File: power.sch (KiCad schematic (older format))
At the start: 25 parts, among them Q1 DMP3099L-7, U3 TPS565201DDC, U5 MCP73223-C2S

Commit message: readability
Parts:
- added J?: Conn_01x02_Male, Connector_JST:JST_SH_BM02B-SRSS-TB_1x02-1MP_P1.00mm_Vertical, symbol Connector:Conn_01x02_Male
- added J?: Conn_01x02_Male, Connector_JST:JST_SH_SM02B-SRSS-TB_1x02-1MP_P1.00mm_Horizontal, symbol Connector:Conn_01x02_Male
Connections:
- net GND: now also J?.2 (Pin_2), J?.2 (Pin_2)
- net VBAT: now also J?.1 (Pin_1), J?.1 (Pin_1)
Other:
- note added: "2 redundant battery connectors.\nconnect only one!"
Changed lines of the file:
@@
 $Descr A4 11693 8268
 encoding utf-8
-Sheet 2 2
+Sheet 2 5
 Title ""
 Date ""
@@
 Wire Wire Line
 	6450 4700 6700 4700
+$Comp
+L Connector:Conn_01x02_Male J?
+U 1 1 606051B8
+P 9800 3600
+F 0 "J?" H 9908 3781 50  0000 C CNN
+F 1 "Conn_01x02_Male" H 9908 3690 50  0000 C CNN
+F 2 "Connector_JST:JST_SH_BM02B-SRSS-TB_1x02-1MP_P1.00mm_Vertical" H 9800 3600 50  0001 C CNN
+F 3 "~" H 9800 3600 50  0001 C CNN
+	1    9800 3600
+	1    0    0    -1
+$EndComp
+Wire Wire Line
+	10000 2800 10000 3600
+Text GLabel 10000 2800 1    118  Input ~ 0
+VBAT
+Wire Wire Line
+	10000 3700 10000 4400
+$Comp
+L power:GND #PWR?
+U 1 1 606051C1
+P 10000 4400
+F 0 "#PWR?" H 10000 4150 50  0001 C CNN
+F 1 "GND" H 10005 4227 50  0000 C CNN
+F 2 "" H 10000 4400 50  0001 C CNN
+F 3 "" H 10000 4400 50  0001 C CNN
+	1    10000 4400
+	1    0    0    -1
+$EndComp
+$Comp
+L Connector:Conn_01x02_Male J?
+U 1 1 606051C7
+P 10600 3600
+F 0 "J?" H 10708 3781 50  0000 C CNN
+F 1 "Conn_01x02_Male" H 10708 3690 50  0000 C CNN
+F 2 "Connector_JST:JST_SH_SM02B-SRSS-TB_1x02-1MP_P1.00mm_Horizontal" H 10600 3600 50  0001 C CNN
+F 3 "~" H 10600 3600 50  0001 C CNN
+	1    10600 3600
+	1    0    0    -1
+$EndComp
+Wire Wire Line
+	10800 2800 10800 3600
+Text GLabel 10800 2800 1    118  Input ~ 0
+VBAT
+Wire Wire Line
+	10800 3700 10800 4400
+$Comp
+L power:GND #PWR?
+U 1 1 606051D0
+P 10800 4400
+F 0 "#PWR?" H 10800 4150 50  0001 C CNN
+F 1 "GND" H 10805 4227 50  0000 C CNN
+F 2 "" H 10800 4400 50  0001 C CNN
+F 3 "" H 10800 4400 50  0001 C CNN
+	1    10800 4400
+	1    0    0    -1
+$EndComp
+Text Notes 9950 2000 0    50   ~ 0
+2 redundant battery connectors.\nconnect only one!
 $EndSCHEMATC

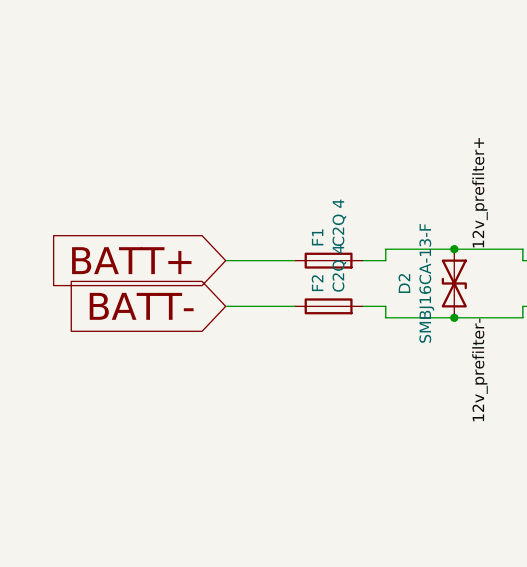
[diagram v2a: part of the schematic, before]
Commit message: Esp32 & Canbus Sch. edited.
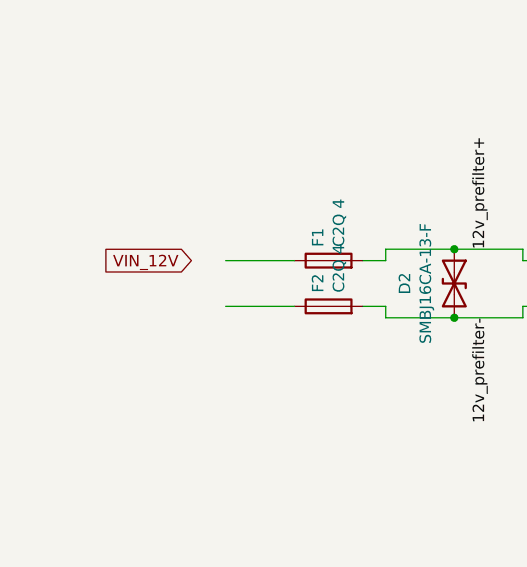
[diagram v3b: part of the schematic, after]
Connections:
- net labels added: VIN_12V
- net labels removed: BATT+, BATT-
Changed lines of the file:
@@
 Wire Wire Line
 	1700 2300 1400 2300
-Text GLabel 1400 2300 0    118  Input ~ 0
-BATT-
-Text GLabel 1400 2100 0    118  Input ~ 0
-BATT+
 Wire Wire Line
 	6900 5000 6900 5150
@@
 Text Notes 9950 2000 0    50   ~ 0
 2 redundant battery connectors.\nconnect only one!
+Text GLabel 1250 2100 0    50   Input ~ 0
+VIN_12V
 $EndSCHEMATC

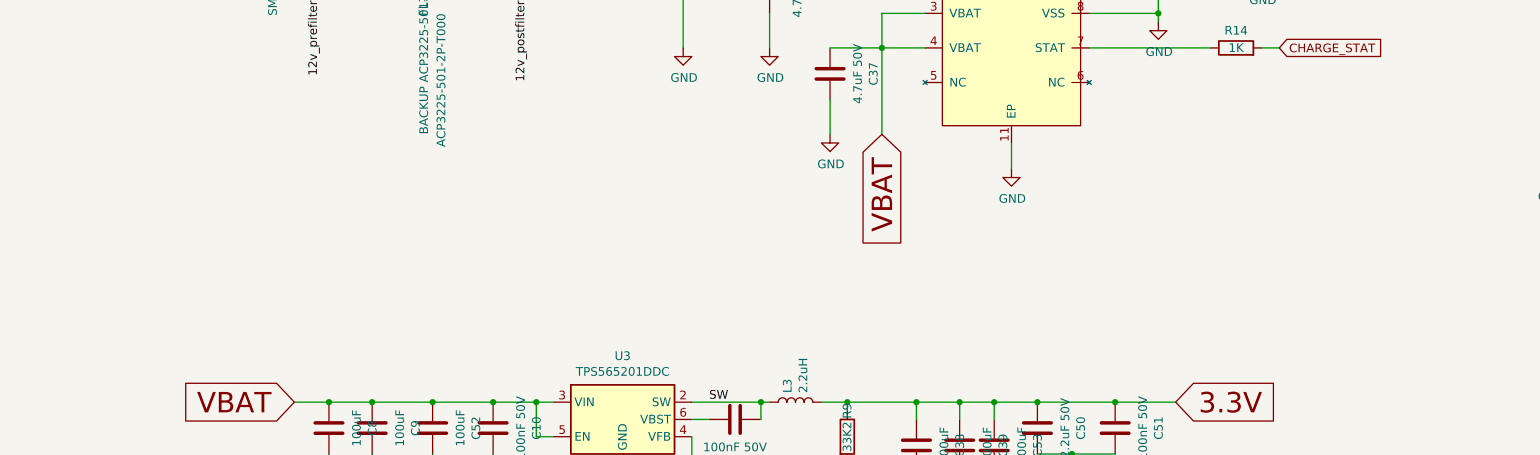
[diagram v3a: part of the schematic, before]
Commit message: Modem schematic updated.
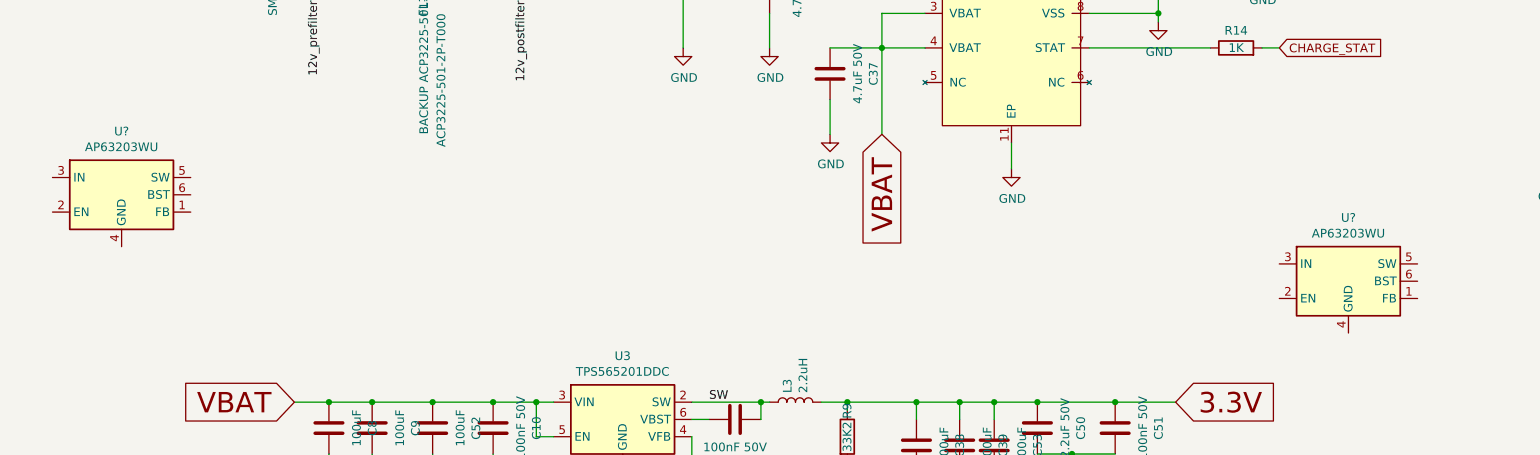
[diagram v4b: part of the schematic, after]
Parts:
- added U? (x2): AP63203WU, Package_TO_SOT_SMD:TSOT-23-6, symbol Regulator_Switching:AP63203WU
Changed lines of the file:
@@
 Text GLabel 1250 2100 0    50   Input ~ 0
 VIN_12V
+$Comp
+L Regulator_Switching:AP63203WU U?
+U 1 1 604E2EDE
+P 1400 3500
+F 0 "U?" H 1400 3867 50  0000 C CNN
+F 1 "AP63203WU" H 1400 3776 50  0000 C CNN
+F 2 "Package_TO_SOT_SMD:TSOT-23-6" H 1400 2600 50  0001 C CNN
+F 3 "https://www.diodes.com/assets/Datasheets/AP63200-AP63201-AP63203-AP63205.pdf" H 1400 3500 50  0001 C CNN
+	1    1400 3500
+	1    0    0    -1
+$EndComp
+$Comp
+L Regulator_Switching:AP63203WU U?
+U 1 1 6069DD08
+P 8500 4000
+F 0 "U?" H 8500 4367 50  0000 C CNN
+F 1 "AP63203WU" H 8500 4276 50  0000 C CNN
+F 2 "Package_TO_SOT_SMD:TSOT-23-6" H 8500 3100 50  0001 C CNN
+F 3 "https://www.diodes.com/assets/Datasheets/AP63200-AP63201-AP63203-AP63205.pdf" H 8500 4000 50  0001 C CNN
+	1    8500 4000
+	1    0    0    -1
+$EndComp
 $EndSCHEMATC

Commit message: Power Sch. Updated.
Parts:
- removed C36, C37: 4.7uF 50V, Capacitor_SMD:C_0603_1608Metric, symbol Device:C
- removed C39, C52, C53, C8: 100uF, Capacitor_SMD:C_1206_3216Metric, symbol Device:C
- removed C51: 100nF 50V, Capacitor_SMD:C_0603_1608Metric, symbol Device:C
- removed F1, F2: C2Q 4, Fuse:Fuse_0603_1608Metric, symbol Device:Fuse
- removed FL2: BACKUP ACP3225-501-2P-T000, aep:ACP3225, symbol Device:EMI_Filter_LL_1423
- removed J?: Conn_01x02_Male, Connector_JST:JST_SH_BM02B-SRSS-TB_1x02-1MP_P1.00mm_Vertical, symbol Connector:Conn_01x02_Male
- removed J?: Conn_01x02_Male, Connector_JST:JST_SH_SM02B-SRSS-TB_1x02-1MP_P1.00mm_Horizontal, symbol Connector:Conn_01x02_Male
- removed L3: 2.2uH, Inductor_SMD:L_Coilcraft_XxL4020, symbol Device:L
- removed Q1: DMP3099L-7, Package_TO_SOT_SMD:SOT-23, symbol Device:Q_PMOS_GSD
- removed R13, R14: 1K, Resistor_SMD:R_0603_1608Metric, symbol Device:R
- removed U3: TPS565201DDC, Package_TO_SOT_SMD:SOT-23-6, symbol Regulator_Switching:TPS565208
- removed U?: AP63203WU, Package_TO_SOT_SMD:TSOT-23-6, symbol Regulator_Switching:AP63203WU
- added C1, C13, C16, C2: 10uF 50V, Capacitor_SMD:C_0805_2012Metric, symbol Device:C
- added C11, C20, C5, C6: 100nF 50V, Capacitor_SMD:C_0603_1608Metric, symbol Device:C
- added C12, C14, C15, C3, C4: 4.7uF, Capacitor_SMD:C_0603_1608Metric, symbol Device:C
- added C17: 100nF, Capacitor_SMD:C_0603_1608Metric, symbol Device:C
- added C19, C21, C23: 22uF 25V, Capacitor_SMD:C_0805_2012Metric, symbol Device:C
- added C22, C24: 100pF 50V, Capacitor_SMD:C_0603_1608Metric, symbol Device:C
- added D2: RS1GTR, Diode_SMD:D_SMA, symbol Device:D_Schottky
- added F1: 0ZCF0030FF2C, Fuse:Fuse_2920_7451Metric_Castellated, symbol Device:Polyfuse_Small
- added J2: Conn_01x02_Male, Connector_JST:JST_SH_BM02B-SRSS-TB_1x02-1MP_P1.00mm_Vertical, symbol Connector:Conn_01x02_Male
- added J3: Conn_01x02_Male, Connector_JST:JST_SH_SM02B-SRSS-TB_1x02-1MP_P1.00mm_Horizontal, symbol Connector:Conn_01x02_Male
- added L1: 1255AY-3R9N=P3, IND_1255AY-3R9N=P3, symbol 1255AY-3R9N_P3:1255AY-3R9N=P3
- added R1, R11, R2, R4: 10k, Resistors:0603, symbol Device:R
- added R10: 3.9k, Resistors:0603, symbol Device:R
- added R3, R5, R7: R0, Resistors:0603, symbol Device:R
- added R6, R8: R0-DNP, Resistors:0603, symbol Device:R
- added TP1, TP2, TP3, TP4, TP5, TP6, TP7: L0, OLIMEX_TestPoints-FP:TP_SMD, symbol Connector:TestPoint_Alt
- added U1, U2: LM66100, Package_TO_SOT_SMD:SOT-363_SC-70-6, symbol pocasicko-cache:Moje_LM66100
- added U3: TLV76750, Package_SON:WSON-6-1EP_2x2mm_P0.65mm_EP1x1.6mm_ThermalVias, symbol aep:TLV767
- C10, C18: value 100nF 50V -> 100nF
- C7: renamed from C50; value 2.2uF 50V -> 100pF 50V
- C8: renamed from C38; value 100uF -> 10uF 50V; footprint Capacitor_SMD:C_1206_3216Metric -> Capacitor_SMD:C_0805_2012Metric
- C9: value 100uF -> 10uF; footprint Capacitor_SMD:C_1206_3216Metric -> Capacitor_SMD:C_0603_1608Metric
- D1: renamed from D2; value SMBJ16CA-13-F -> SMBJ16CA-Q
- R12: value 10K -> 10k; footprint Resistor_SMD:R_0603_1608Metric -> Resistors:0603
- R9: value 33K2 -> R0-DNP; footprint Resistor_SMD:R_0603_1608Metric -> Resistors:0603
- U5: value MCP73223-C2S -> MCP73123-22S
- gave numbers to parts that had none: 1
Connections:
- net labels added: +12V, +3V3, +5V, +BATT, 12V_FILTER_IN, 3V3_BUCK, CHARGER_EN, VIN_GND
- net labels removed: 12v_postfilter+, 12v_postfilter-, 12v_prefilter+, 12v_prefilter-, 3.3V, SW, V12_safe, VBAT
- wire segments 103 -> 138
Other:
- note added: "Batt. Charger 5V Supply"
- note added: "Feedback resistors for \nAP63200 ADJ. Version"
- note added: "LiFePo4 Charger"
- note added: "Main 3V3 Buck Conv."
- note added: "Main Input Filter & Protection"
- note added: "Power Supply Switchover"
- note removed: "TVS clamp to 26V\n"
- moved on the sheet: C7, C8, D1, FL1, U4

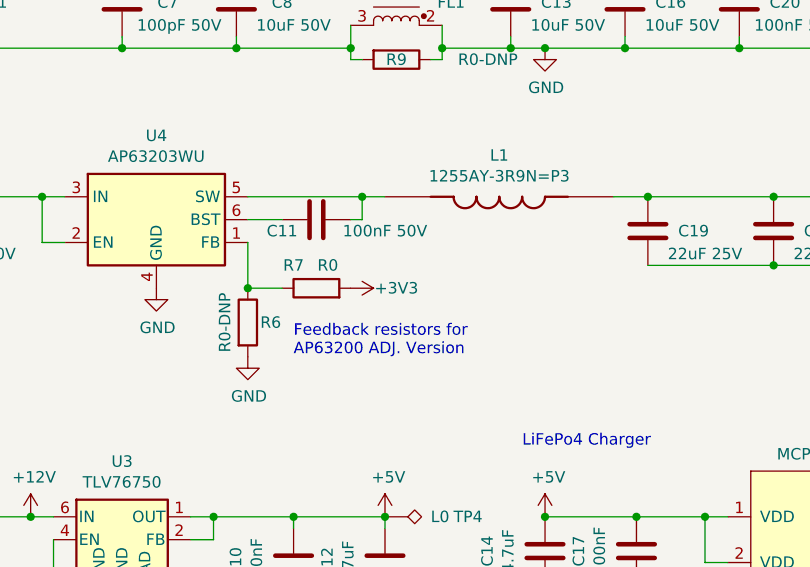
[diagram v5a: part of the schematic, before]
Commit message: Fixed Buck feedback reference.
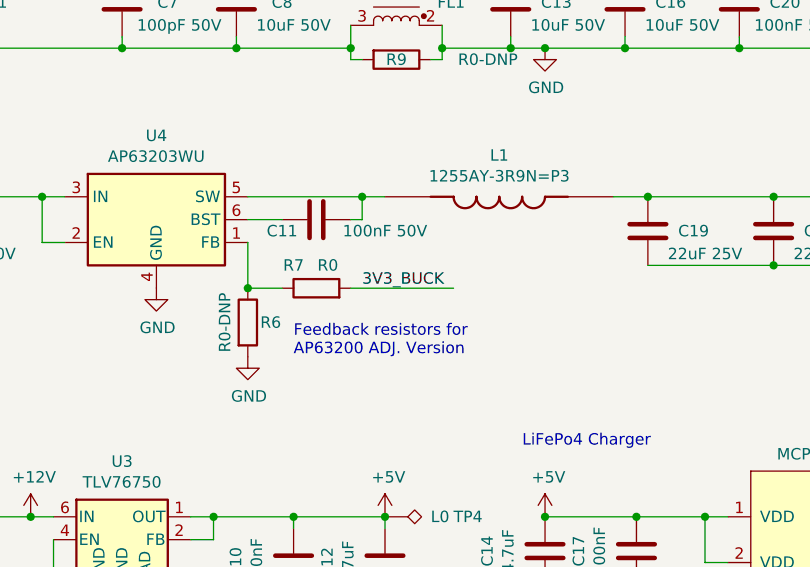
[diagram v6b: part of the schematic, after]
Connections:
- net +3V3: no longer R7.2
- net 3V3_BUCK: now also R7.2
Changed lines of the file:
@@
 	1    0    0    -1
-$EndComp
-$Comp
-L power:+3V3 #PWR?
-U 1 1 6054766C
-P 4150 3000
-AR Path="/606146CD/6054766C" Ref="#PWR?"  Part="1"
-AR Path="/603B75FA/6054766C" Ref="#PWR?"  Part="1"
-AR Path="/603BB897/6054766C" Ref="#PWR?"  Part="1"
-AR Path="/6055B0F2/6054766C" Ref="#PWR?"  Part="1"
-AR Path="/60856F71/6054766C" Ref="#PWR021"  Part="1"
-F 0 "#PWR021" H 4150 2850 50  0001 C CNN
-F 1 "+3V3" V 4150 3200 50  0000 C CNN
-F 2 "" H 4150 3000 50  0001 C CNN
-F 3 "" H 4150 3000 50  0001 C CNN
-	1    4150 3000
-	0    1    1    0
 $EndComp
 Text Notes 3900 3300 0    50   ~ 0
@@
 Wire Wire Line
 	5250 4750 5000 4750
+Text Label 4200 3000 0    50   ~ 0
+3V3_BUCK
+Wire Wire Line
+	4150 3000 4600 3000
 $EndSCHEMATC
